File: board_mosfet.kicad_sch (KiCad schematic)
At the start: 13 parts, among them J2 USB_IN, J3 USB_OUT, Q1 Q_NMOS_GDS, Q2 Q_NMOS_GDS, U1 AMS1117-3.3, U2 INA219AxD, U3 INA219AxD

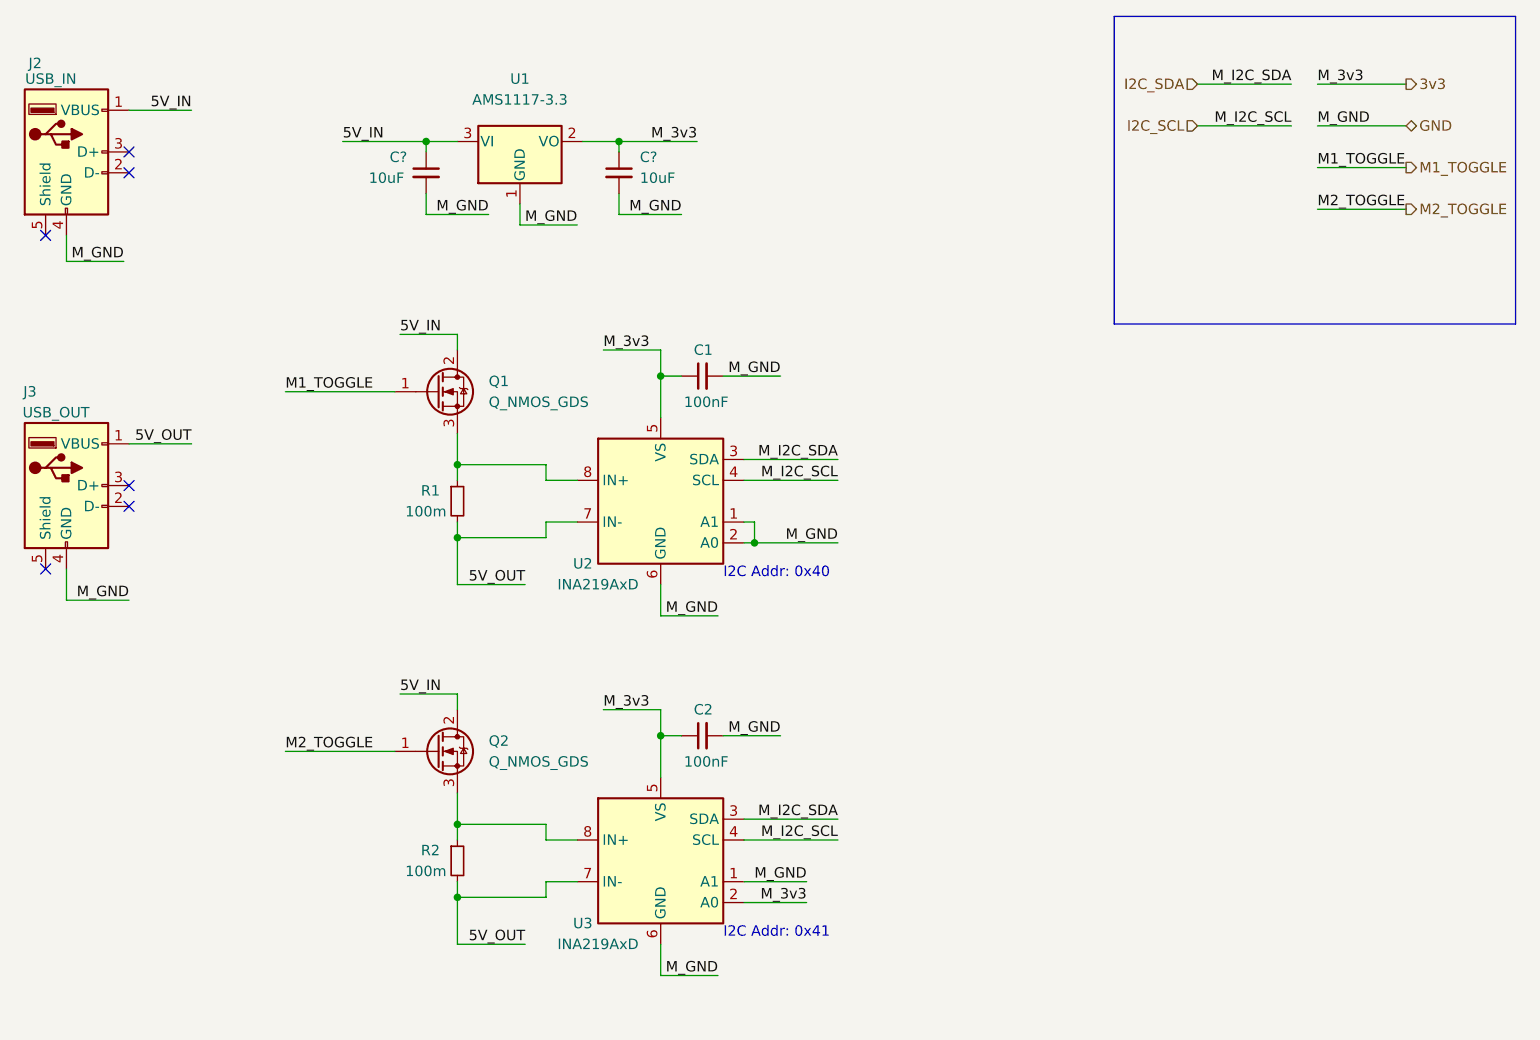
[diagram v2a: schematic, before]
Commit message: Updated board connections. Added supplier info for all parts
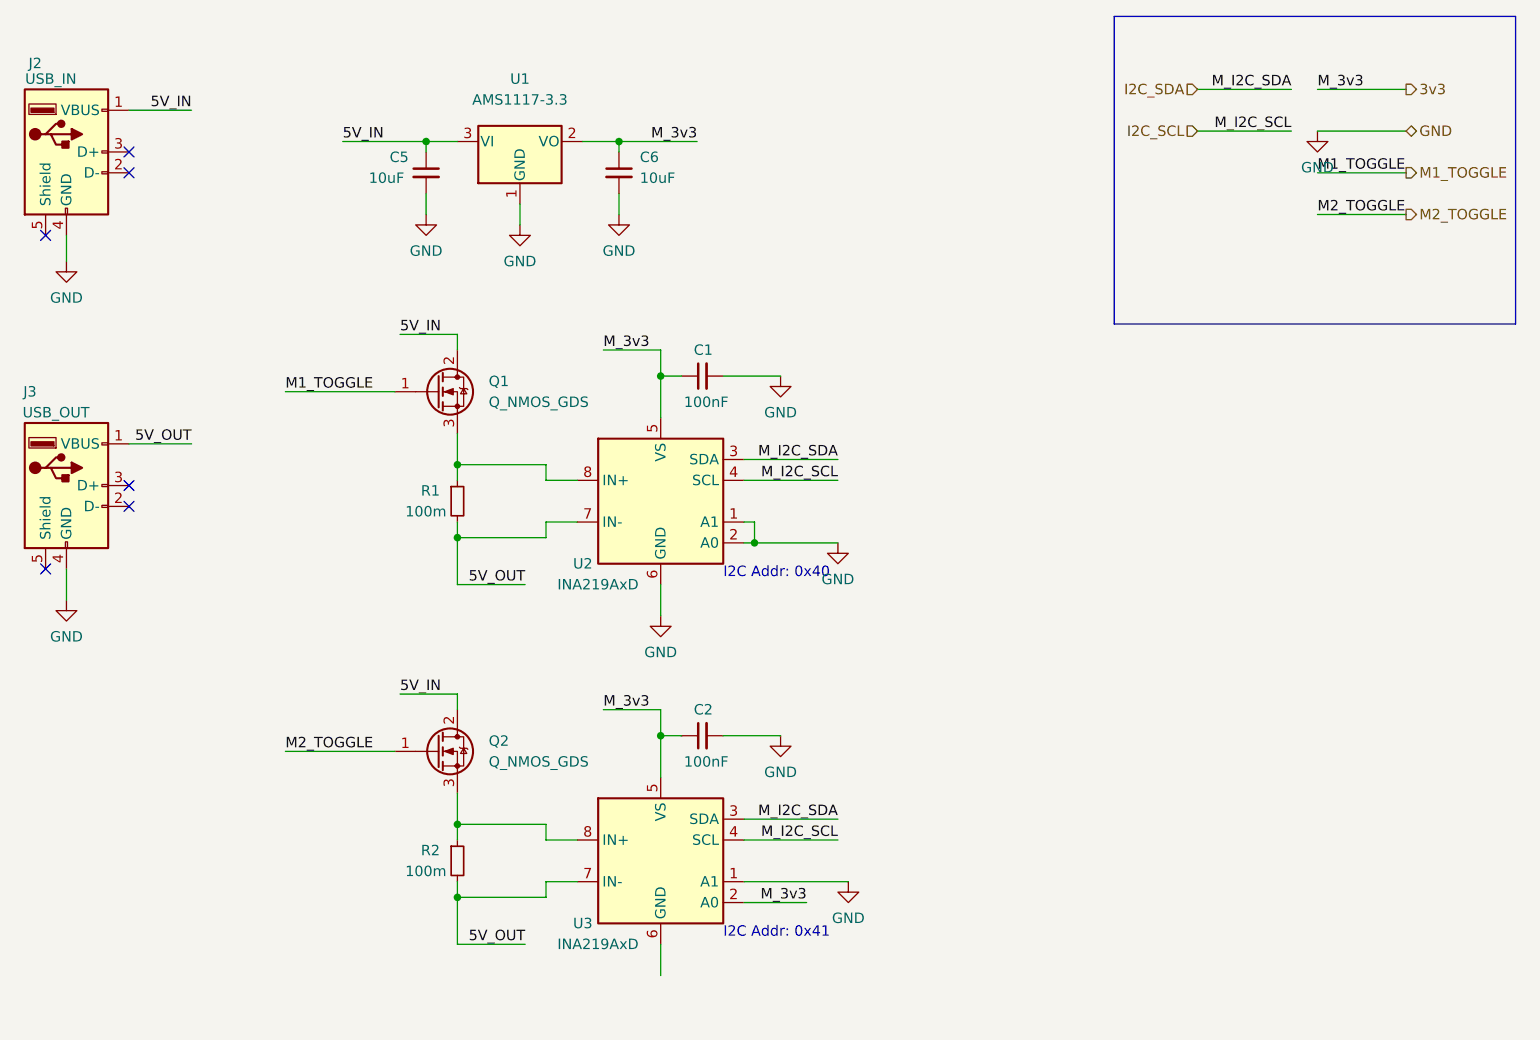
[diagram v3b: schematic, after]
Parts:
- C1, C2: footprint Capacitor_SMD:C_0402_1005Metric -> Capacitor_SMD:C_0603_1608Metric; LCSC Part Number (none) -> C30926; Manufacturer (none) -> FH (Guangdong Fenghua Advanced Tech); Manufacturer Part Number (none) -> 0603B104K500NT
- C5, C6: renamed from C?; footprint (none) -> Capacitor_SMD:C_0603_1608Metric; LCSC Part Number (none) -> C100042; Manufacturer (none) -> YAGEO; Manufacturer Part Number (none) -> CC0603KRX7R9BB103
- J2: footprint (none) -> Library:U217-041N-4BV81; LCSC Part Number (none) -> C319178; Manufacturer (none) -> XKB Connectivity; Manufacturer Part Number (none) -> U217-041N-4BV81
- J3: footprint (none) -> Library:904-131A2032S10100; LCSC Part Number (none) -> C8328; Manufacturer (none) -> Jing Extension of the Electronic Co.; Manufacturer Part Number (none) -> 904-131A2032S10100
- Q1, Q2: footprint (none) -> Library:YJL3400A
- R1, R2: footprint Resistor_SMD:R_0402_1005Metric -> Resistor_SMD:R_2010_5025Metric; LCSC Part Number (none) -> C474250; Manufacturer (none) -> UNI-ROYAL(Uniroyal Elec); Manufacturer Part Number (none) -> 201007F100LT4E
- U2, U3: LCSC Part Number (none) -> C138706; Manufacturer (none) -> Texas Instruments; Manufacturer Part Number (none) -> INA219AIDR
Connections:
- net GND: no longer U3.6 (GND)

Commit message: Did work on schematic
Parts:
- added J5: USB_OUT, Library:904-131A2032S10100, symbol Connector:USB_A
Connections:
- net GND: now also U3.6 (GND), J5.4 (GND)
- net 5V_OUT renamed 5V_OUT_1
- net 5V_OUT_1: no longer R2.2, U3.7 (IN-)
- new net 5V_OUT_2: J5.1 (VBUS), R2.2, U3.7 (IN-)
- no-connect marks 6 -> 9
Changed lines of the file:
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@@
   (no_connect (at 34.925 95.885))
   (no_connect (at 34.925 55.245))
+  (no_connect (at 34.925 132.08))
+  (no_connect (at 45.085 121.92))
+  (no_connect (at 45.085 124.46))
   (wire (pts (xy 85.09 83.185) (xy 95.885 83.185))
     (stroke (width 0) (type default) (color 0 0 0 0))
@@
     (stroke (width 0) (type default) (color 0 0 0 0))
   )
-  (wire (pts (xy 93.345 141.605) (xy 85.09 141.605))
+  (wire (pts (xy 95.25 141.605) (xy 85.09 141.605))
     (stroke (width 0) (type default) (color 0 0 0 0))
   )
@@
     (stroke (width 0) (type default) (color 0 0 0 0))
   )
-  (wire (pts (xy 93.345 97.79) (xy 85.09 97.79))
+  (wire (pts (xy 95.25 97.79) (xy 85.09 97.79))
     (stroke (width 0) (type default) (color 0 0 0 0))
   )
@@
     (stroke (width 0) (type default) (color 0 0 0 0))
   )
-  (wire (pts (xy 45.085 80.645) (xy 52.705 80.645))
+  (wire (pts (xy 45.085 80.645) (xy 55.88 80.645))
     (stroke (width 0) (type default) (color 0 0 0 0))
   )
@@
     (stroke (width 0) (type default) (color 0 0 0 0))
   )
+  (wire (pts (xy 45.085 116.84) (xy 55.88 116.84))
+    (stroke (width 0) (type default) (color 0 0 0 0))
+  )
   (wire (pts (xy 95.885 85.09) (xy 95.885 83.185))
     (stroke (width 0) (type default) (color 0 0 0 0))
@@
     (stroke (width 0) (type default) (color 0 0 0 0))
   )
+  (wire (pts (xy 37.465 132.08) (xy 37.465 135.89))
+    (stroke (width 0) (type default) (color 0 0 0 0))
+  )
   (wire (pts (xy 104.775 43.815) (xy 104.775 45.085))
     (stroke (width 0) (type default) (color 0 0 0 0))
@@
     (effects (font (size 1.27 1.27)) (justify left bottom))
   )
-  (label "5V_OUT" (at 52.705 80.645 180)
-    (effects (font (size 1.27 1.27)) (justify right bottom))
-  )
   (label "M_3v3" (at 127.635 136.525 180)
     (effects (font (size 1.27 1.27)) (justify right bottom))
@@
     (effects (font (size 1.27 1.27)) (justify right bottom))
   )
+  (label "5V_OUT_2" (at 55.88 116.84 180)
+    (effects (font (size 1.27 1.27)) (justify right bottom))
+  )
   (label "M2_TOGGLE" (at 189.865 52.705 0)
     (effects (font (size 1.27 1.27)) (justify left bottom))
@@
     (effects (font (size 1.27 1.27)) (justify left bottom))
   )
-  (label "5V_OUT" (at 93.345 141.605 180)
-    (effects (font (size 1.27 1.27)) (justify right bottom))
-  )
-  (label "5V_OUT" (at 93.345 97.79 180)
+  (label "5V_OUT_2" (at 95.25 141.605 180)
+    (effects (font (size 1.27 1.27)) (justify right bottom))
+  )
+  (label "5V_OUT_1" (at 95.25 97.79 180)
     (effects (font (size 1.27 1.27)) (justify right bottom))
   )
   (label "5V_IN" (at 71.12 43.815 0)
     (effects (font (size 1.27 1.27)) (justify left bottom))
+  )
+  (label "5V_OUT_1" (at 55.88 80.645 180)
+    (effects (font (size 1.27 1.27)) (justify right bottom))
   )
   (label "M_I2C_SDA" (at 131.445 82.55 180)
@@
     (pin "2")
   )
+  (symbol (lib_id "power:GND") (at 37.465 135.89 0) (unit 1)
+    (in_bom yes) (on_board yes) (fields_autoplaced)
+    (property "Reference" "#PWR018" (id 0) (at 37.465 142.24 0)
+      (effects (font (size 1.27 1.27)) hide)
+    )
+    (property "Value" "GND" (id 1) (at 37.465 140.335 0))
+    (property "Footprint" "" (id 2) (at 37.465 135.89 0)
+      (effects (font (size 1.27 1.27)) hide)
+    )
+    (property "Datasheet" "" (id 3) (at 37.465 135.89 0)
+      (effects (font (size 1.27 1.27)) hide)
+    )
+    (pin "1")
+  )
   (symbol (lib_id "power:GND") (at 124.46 72.39 0) (unit 1)
     (in_bom yes) (on_board yes) (fields_autoplaced)
@@
     )
     (property "Datasheet" "" (id 3) (at 124.46 72.39 0)
+      (effects (font (size 1.27 1.27)) hide)
+    )
+    (pin "1")
+  )
+  (symbol (lib_id "power:GND") (at 109.855 145.415 0) (unit 1)
+    (in_bom yes) (on_board yes) (fields_autoplaced)
+    (property "Reference" "#PWR?" (id 0) (at 109.855 151.765 0)
+      (effects (font (size 1.27 1.27)) hide)
+    )
+    (property "Value" "GND" (id 1) (at 109.855 149.86 0))
+    (property "Footprint" "" (id 2) (at 109.855 145.415 0)
+      (effects (font (size 1.27 1.27)) hide)
+    )
+    (property "Datasheet" "" (id 3) (at 109.855 145.415 0)
       (effects (font (size 1.27 1.27)) hide)
     )
@@
     (pin "8")
   )
+  (symbol (lib_id "Connector:USB_A") (at 37.465 121.92 0) (unit 1)
+    (in_bom yes) (on_board yes)
+    (property "Reference" "J5" (id 0) (at 33.02 110.49 0))
+    (property "Value" "USB_OUT" (id 1) (at 36.195 113.03 0))
+    (property "Footprint" "Library:904-131A2032S10100" (id 2) (at 41.275 123.19 0)
+      (effects (font (size 1.27 1.27)) hide)
+    )
+    (property "Datasheet" " ~" (id 3) (at 41.275 123.19 0)
+      (effects (font (size 1.27 1.27)) hide)
+    )
+    (property "LCSC Part Number" "C8328" (id 4) (at 37.465 121.92 0)
+      (effects (font (size 1.27 1.27)) hide)
+    )
+    (property "Manufacturer" "Jing Extension of the Electronic Co." (id 5) (at 37.465 121.92 0)
+      (effects (font (size 1.27 1.27)) hide)
+    )
+    (property "Manufacturer Part Number" "904-131A2032S10100" (id 6) (at 37.465 121.92 0)
+      (effects (font (size 1.27 1.27)) hide)
+    )
+    (pin "1")
+    (pin "2")
+    (pin "3")
+    (pin "4")
+    (pin "5")
+  )
   (symbol (lib_id "power:GND") (at 81.28 52.705 0) (unit 1)

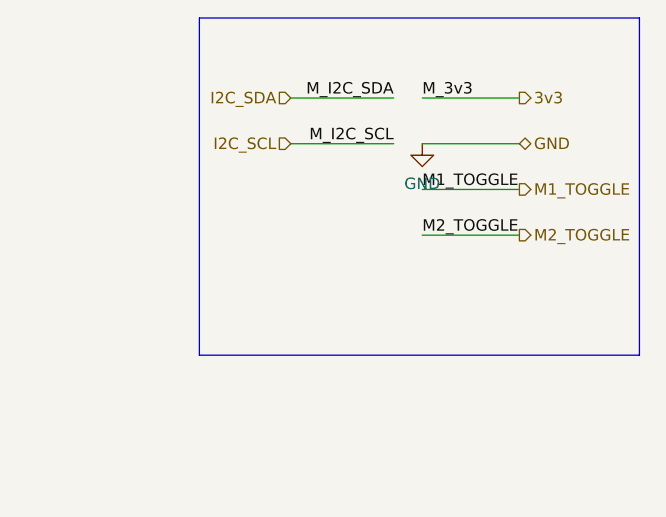
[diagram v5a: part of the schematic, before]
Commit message: Added TX/RX to schematic. Updated PCB
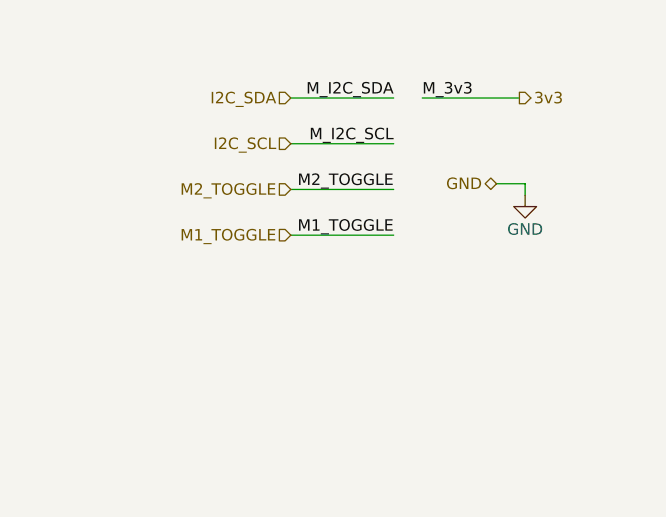
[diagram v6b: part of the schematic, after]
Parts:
- U1: LCSC Part Number C173386 -> C347222; Manufacturer Shenzhen Fuman Elec -> UMW(Youtai Semiconductor Co., Ltd.); Manufacturer Part Number AMS1117-3.3V -> AMS1117-3.3
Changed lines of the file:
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@@
-    (stroke (width 0) (type default) (color 0 0 0 0))
-  )
-  (polyline (pts (xy 213.995 28.575) (xy 213.995 66.04))
     (stroke (width 0) (type default) (color 0 0 0 0))
   )
@@
     (stroke (width 0) (type default) (color 0 0 0 0))
   )
-  (wire (pts (xy 189.865 47.625) (xy 200.66 47.625))
+  (wire (pts (xy 186.69 52.705) (xy 175.26 52.705))
     (stroke (width 0) (type default) (color 0 0 0 0))
   )
@@
     (stroke (width 0) (type default) (color 0 0 0 0))
   )
-  (polyline (pts (xy 213.995 66.04) (xy 165.1 66.04))
-    (stroke (width 0) (type default) (color 0 0 0 0))
-  )
-  (wire (pts (xy 189.865 42.545) (xy 200.66 42.545))
+  (wire (pts (xy 201.295 46.99) (xy 198.12 46.99))
     (stroke (width 0) (type default) (color 0 0 0 0))
   )
@@
     (stroke (width 0) (type default) (color 0 0 0 0))
   )
-  (polyline (pts (xy 165.1 28.575) (xy 213.995 28.575))
-    (stroke (width 0) (type default) (color 0 0 0 0))
-  )
   (wire (pts (xy 109.855 141.605) (xy 109.855 145.415))
     (stroke (width 0) (type default) (color 0 0 0 0))
   )
-  (polyline (pts (xy 165.1 28.575) (xy 165.1 66.04))
-    (stroke (width 0) (type default) (color 0 0 0 0))
-  )
   (wire (pts (xy 120.015 133.985) (xy 132.715 133.985))
     (stroke (width 0) (type default) (color 0 0 0 0))
@@
     (stroke (width 0) (type default) (color 0 0 0 0))
   )
+  (wire (pts (xy 201.295 46.99) (xy 201.295 48.26))
+    (stroke (width 0) (type default) (color 0 0 0 0))
+  )
   (wire (pts (xy 120.015 92.71) (xy 121.285 92.71))
     (stroke (width 0) (type default) (color 0 0 0 0))
@@
     (stroke (width 0) (type default) (color 0 0 0 0))
   )
-  (wire (pts (xy 189.865 52.705) (xy 200.66 52.705))
+  (wire (pts (xy 186.69 47.625) (xy 175.26 47.625))
     (stroke (width 0) (type default) (color 0 0 0 0))
   )
@@
     (effects (font (size 1.27 1.27)) (justify right bottom))
   )
-  (label "M1_TOGGLE" (at 189.865 47.625 0)
-    (effects (font (size 1.27 1.27)) (justify left bottom))
+  (label "M1_TOGGLE" (at 186.69 52.705 180)
+    (effects (font (size 1.27 1.27)) (justify right bottom))
   )
   (label "M_3v3" (at 114.3 43.815 180)
@@
     (effects (font (size 1.27 1.27)) (justify right bottom))
   )
-  (label "M2_TOGGLE" (at 189.865 52.705 0)
-    (effects (font (size 1.27 1.27)) (justify left bottom))
+  (label "M2_TOGGLE" (at 186.69 47.625 180)
+    (effects (font (size 1.27 1.27)) (justify right bottom))
   )
   (label "M_I2C_SDA" (at 131.445 126.365 180)
@@
     (effects (font (size 1.27 1.27)) (justify right bottom))
   )
-  (hierarchical_label "GND" (shape bidirectional) (at 200.66 42.545 0)
-    (effects (font (size 1.27 1.27)) (justify left))
+  (hierarchical_label "GND" (shape bidirectional) (at 198.12 46.99 180)
+    (effects (font (size 1.27 1.27)) (justify right))
   )
   (hierarchical_label "I2C_SCL" (shape input) (at 175.26 42.545 180)
@@
     (effects (font (size 1.27 1.27)) (justify left))
   )
-  (hierarchical_label "M2_TOGGLE" (shape output) (at 200.66 52.705 0)
-    (effects (font (size 1.27 1.27)) (justify left))
+  (hierarchical_label "M2_TOGGLE" (shape input) (at 175.26 47.625 180)
+    (effects (font (size 1.27 1.27)) (justify right))
   )
   (hierarchical_label "I2C_SDA" (shape input) (at 175.26 37.465 180)
     (effects (font (size 1.27 1.27)) (justify right))
   )
-  (hierarchical_label "M1_TOGGLE" (shape output) (at 200.66 47.625 0)
-    (effects (font (size 1.27 1.27)) (justify left))
+  (hierarchical_label "M1_TOGGLE" (shape input) (at 175.26 52.705 180)
+    (effects (font (size 1.27 1.27)) (justify right))
   )
   (symbol (lib_id "power:GND") (at 104.775 52.705 0) (unit 1)
@@
     (pin "2")
   )
-  (symbol (lib_id "power:GND") (at 189.865 42.545 0) (unit 1)
-    (in_bom yes) (on_board yes) (fields_autoplaced)
-    (property "Reference" "#PWR011" (id 0) (at 189.865 48.895 0)
-      (effects (font (size 1.27 1.27)) hide)
-    )
-    (property "Value" "GND" (id 1) (at 189.865 46.99 0))
-    (property "Footprint" "" (id 2) (at 189.865 42.545 0)
-      (effects (font (size 1.27 1.27)) hide)
-    )
-    (property "Datasheet" "" (id 3) (at 189.865 42.545 0)
+  (symbol (lib_id "power:GND") (at 201.295 48.26 0) (unit 1)
+    (in_bom yes) (on_board yes)
+    (property "Reference" "#PWR011" (id 0) (at 201.295 54.61 0)
+      (effects (font (size 1.27 1.27)) hide)
+    )
+    (property "Value" "GND" (id 1) (at 201.295 52.07 0))
+    (property "Footprint" "" (id 2) (at 201.295 48.26 0)
+      (effects (font (size 1.27 1.27)) hide)
+    )
+    (property "Datasheet" "" (id 3) (at 201.295 48.26 0)
       (effects (font (size 1.27 1.27)) hide)
     )
@@
       (effects (font (size 1.27 1.27)) hide)
     )
-    (property "LCSC Part Number" "C173386" (id 4) (at 92.71 43.815 0)
-      (effects (font (size 1.27 1.27)) hide)
-    )
-    (property "Manufacturer" "Shenzhen Fuman Elec" (id 5) (at 92.71 43.815 0)
-      (effects (font (size 1.27 1.27)) hide)
-    )
-    (property "Manufacturer Part Number" "AMS1117-3.3V" (id 6) (at 92.71 43.815 0)
-      (effects (font (size 1.27 1.27)) hide)
-    )
+    (property "LCSC Part Number" "C347222" (id 4) (at 92.71 43.815 0)
+      (effects (font (size 1.27 1.27)) hide)
+    )
+    (property "Manufacturer" "UMW(Youtai Semiconductor Co., Ltd.)" (id 5) (at 92.71 43.815 0)
+      (effects (font (size 1.27 1.27)) hide)
+    )
+    (property "Manufacturer Part Number" "AMS1117-3.3" (id 6) (at 92.71 43.815 0)
+      (effects (font (size 1.27 1.27)) hide)
+    )
